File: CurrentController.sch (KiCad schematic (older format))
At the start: 0 parts

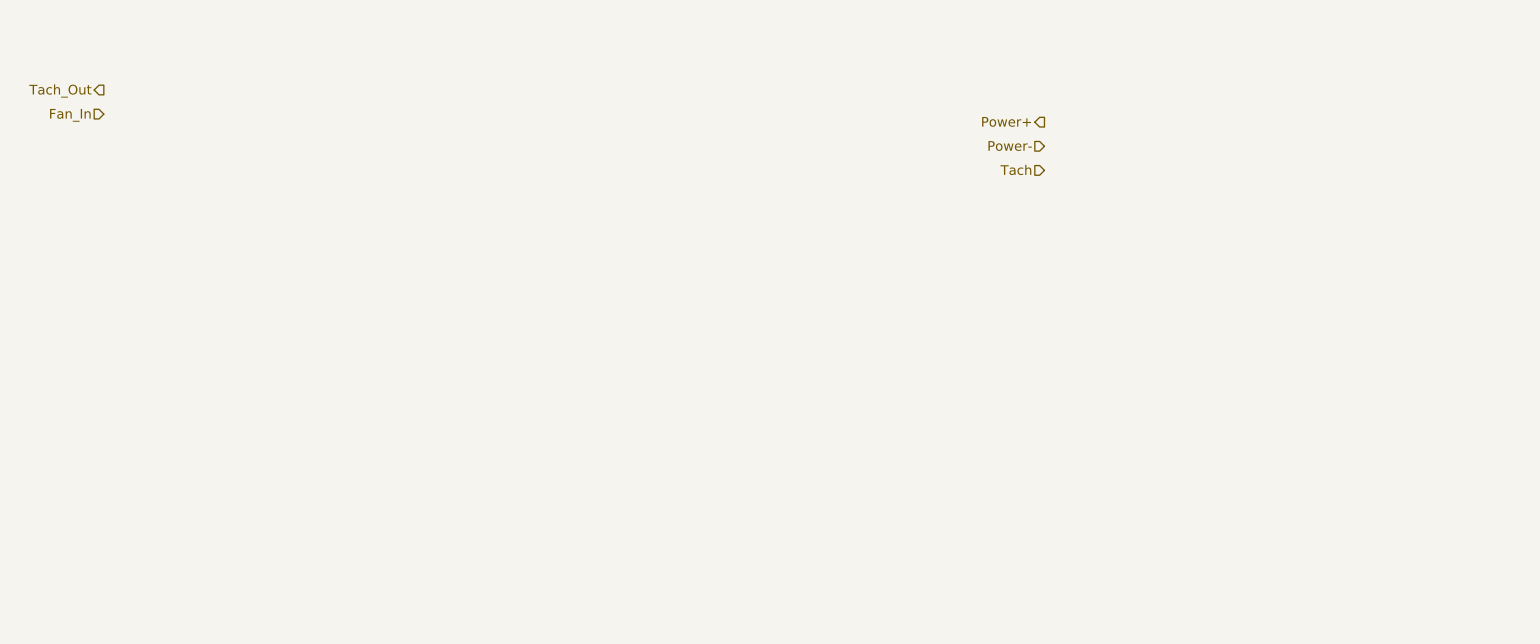
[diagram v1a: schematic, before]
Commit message: understanding the current/fan driver module
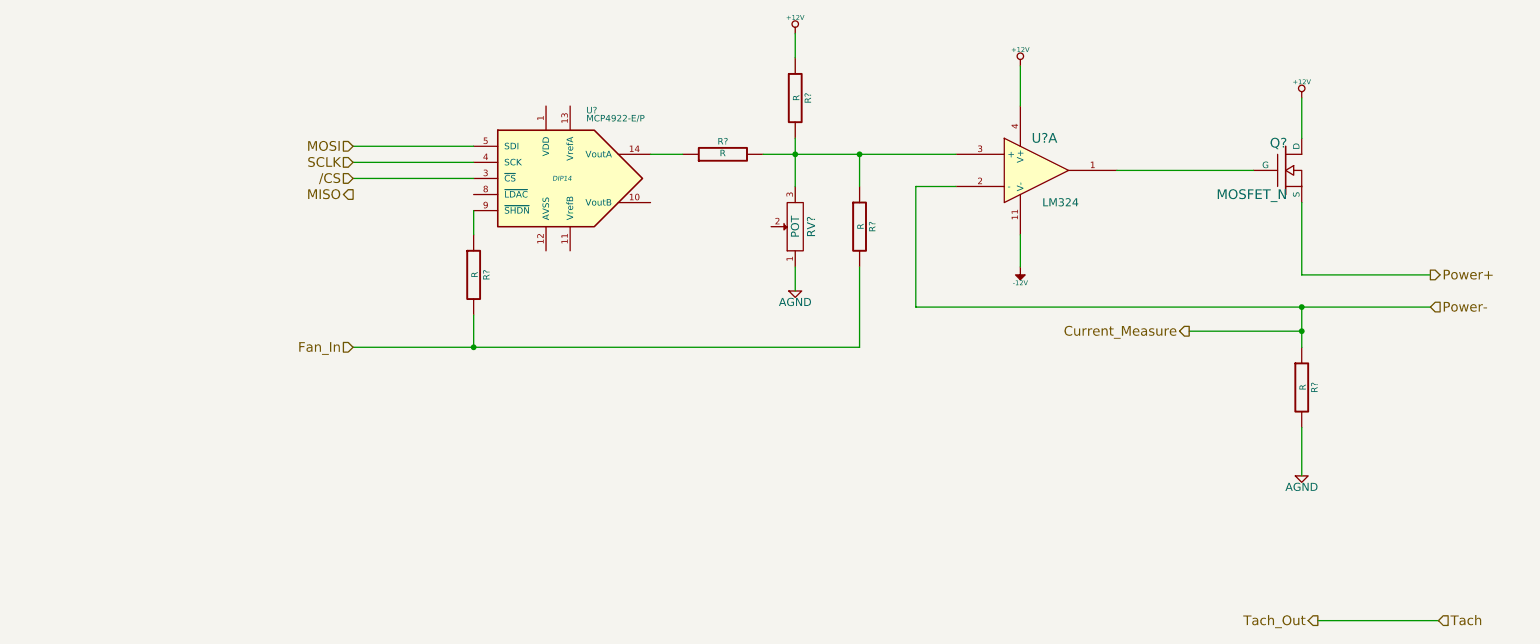
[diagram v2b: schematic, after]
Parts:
- added Q?: MOSFET_N, ~, symbol MOSFET_N
- added R? (x5): R, ~, symbol R
- added RV?: POT, ~, symbol POT
- added U?: LM324, symbol LM324
- added U?: MCP4922-E/P, DIP14, symbol MCP4922-E/P
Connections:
- net Fan_In: now also R?.2, R?.2
- net Power+: now also Q?.S
- new net: Q?.G, U?.1
- new net: R?.1, R?.2, R?.2, RV?.3, U?.3 (+)
- new net: R?.1, U?.14 (VoutA)
- new net: R?.1, U?.9 (~SHDN~)
- new net +12V: Q?.D, R?.1, U?.4 (V+)
- new net -12V: U?.11 (V-)
- new net /CS: U?.3 (~CS~)
- new net AGND: R?.2, RV?.1
- new net Current_Measure: R?.1, U?.2 (-)
- new net MOSI: U?.5 (SDI)
- new net SCLK: U?.4 (SCK)

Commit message: Arduino Module
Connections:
- net Current_Measure renamed CURR_MEAS
- net Fan_In renamed /FAN_EN
- net Power+ renamed FAN_OUT+
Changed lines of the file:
@@
 $Descr A4 11693 8268
 encoding utf-8
-Sheet 7 9
+Sheet 9 9
 Title ""
 Date "30 sep 2013"
@@
 $EndDescr
 Text HLabel 10300 2850 2    60   Output ~ 0
-Power+
-Text HLabel 10300 3050 2    60   Input ~ 0
-Power-
+FAN_OUT+
+Text HLabel 10300 3050 2    60   Output ~ 0
+FAN_OUT-
 Text HLabel 10350 5000 2    60   Input ~ 0
-Tach
+TACH_IN
 Text HLabel 9600 5000 0    60   Output ~ 0
-Tach_Out
+TACH_MEAS
 Text HLabel 3600 3300 0    60   Input ~ 0
-Fan_In
+/FAN_EN
 $Comp
 L LM324 U?
@@
 	10350 5000 9600 5000
 Text HLabel 8800 3200 0    60   Output ~ 0
-Current_Measure
+CURR_MEAS
 Wire Wire Line
 	8800 3200 9500 3200
